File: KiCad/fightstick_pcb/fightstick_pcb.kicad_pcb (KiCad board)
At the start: 2 copper layers, 52 x 51 mm, 34 parts, among them J1 USB_B_Micro, J2 Conn_01x02, J3 Conn_02x18_Odd_Even, J4 Conn_02x18_Odd_Even, U1 NCP1117-3.3_SOT223, U2 W25Q128JVS, U3 RP2040, Y1 ABM8-272-T3

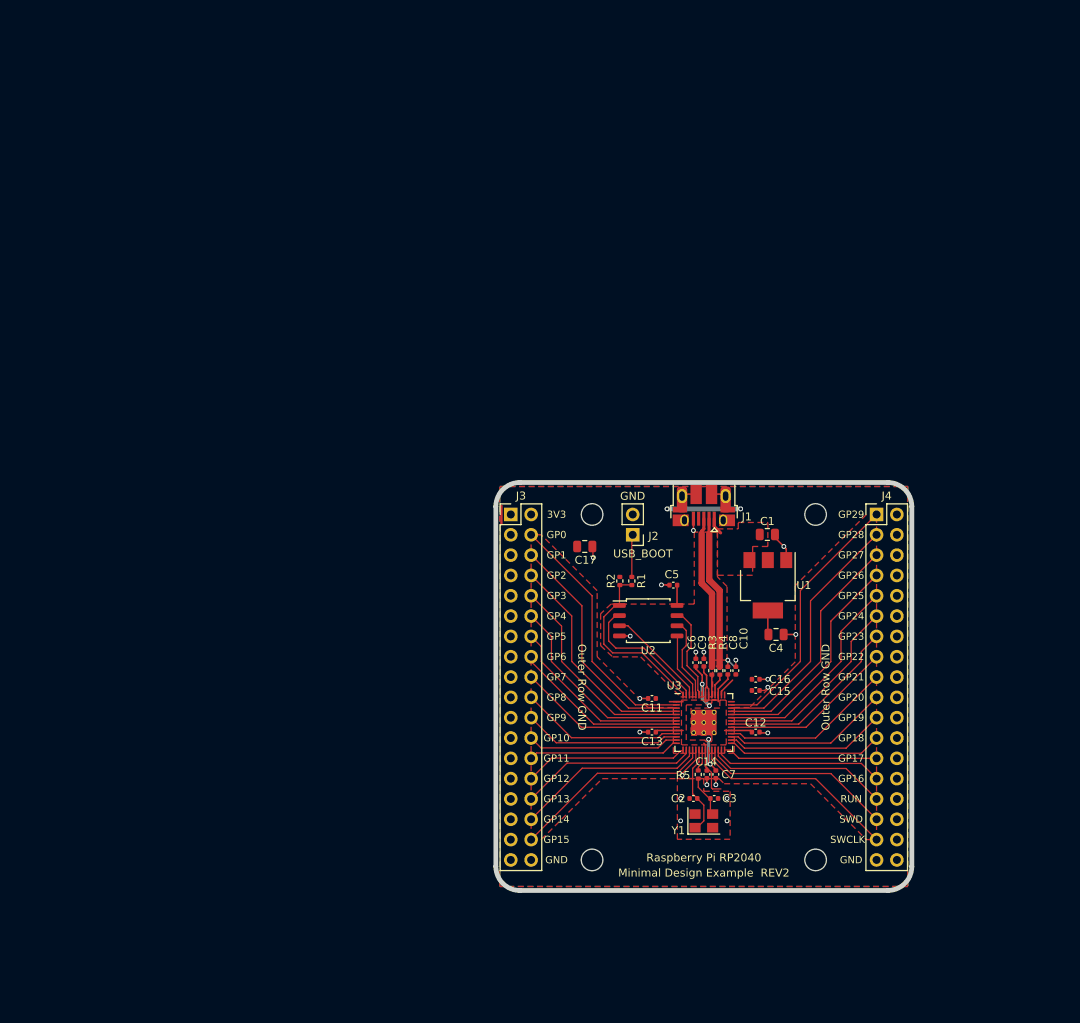
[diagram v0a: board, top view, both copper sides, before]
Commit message: Recreation of minimal design
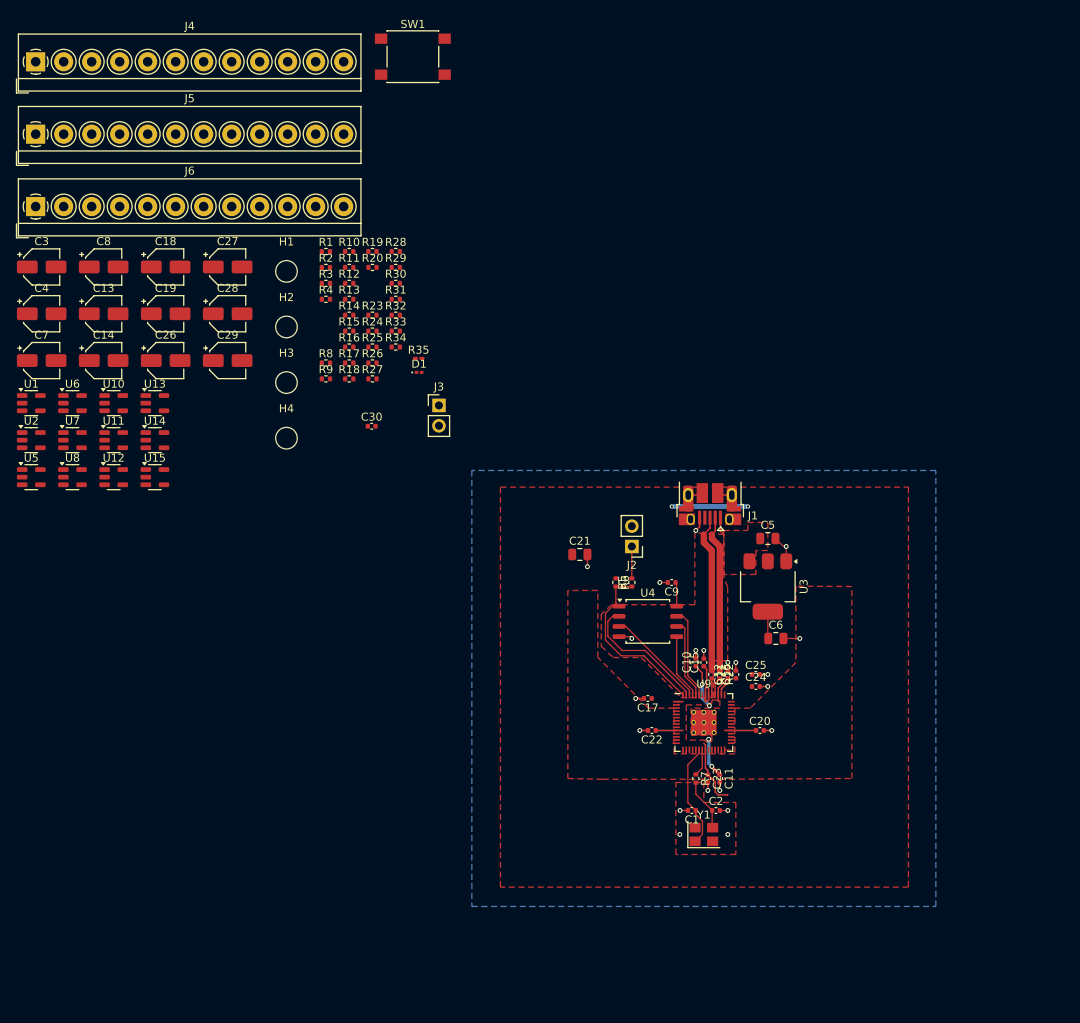
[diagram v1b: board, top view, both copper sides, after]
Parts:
- added C18: 1u, Capacitor_SMD:CP_Elec_4x3, F.Cu at (32.7, 43.1)
- added C19: 1u, Capacitor_SMD:CP_Elec_4x3, F.Cu at (32.7, 48.9)
- added C20: 100n, Capacitor_SMD:C_0402_1005Metric, F.Cu at (107.0, 101.0)
- added C21: 10u, Capacitor_SMD:C_0805_2012Metric, F.Cu at (84.5, 79.0)
- added C22: 100n, Capacitor_SMD:C_0402_1005Metric, F.Cu at (93.5, 101.0)
- added C23: 100n, Capacitor_SMD:C_0402_1005Metric, F.Cu at (100.5, 107.0)
- added C24: 100n, Capacitor_SMD:C_0402_1005Metric, F.Cu at (106.5, 95.5)
- added C25: 100n, Capacitor_SMD:C_0402_1005Metric, F.Cu at (106.5, 94.0)
- added C26: 1u, Capacitor_SMD:CP_Elec_4x3, F.Cu at (32.7, 54.8)
- added C27: 1u, Capacitor_SMD:CP_Elec_4x3, F.Cu at (40.5, 43.1)
- added C28: 1u, Capacitor_SMD:CP_Elec_4x3, F.Cu at (40.5, 48.9)
- added C29: 1u, Capacitor_SMD:CP_Elec_4x3, F.Cu at (40.5, 54.8)
- added C30: 100n, Capacitor_SMD:C_0402_1005Metric, F.Cu at (58.5, 63.0)
- added D1: GREEN, LED_SMD:LED_0201_0603Metric, F.Cu at (64.4, 56.2)
- added J5: Screw_Terminal_01x12, TerminalBlock_4Ucon:TerminalBlock_4Ucon_1x12_P3.50mm_Horizontal, F.Cu at (16.5, 26.5)
- added J6: Screw_Terminal_01x12, TerminalBlock_4Ucon:TerminalBlock_4Ucon_1x12_P3.50mm_Horizontal, F.Cu at (16.5, 35.5)
- added R10: 1k, Resistor_SMD:R_0402_1005Metric, F.Cu at (55.7, 41.1)
- added R11: 1k, Resistor_SMD:R_0402_1005Metric, F.Cu at (55.7, 43.1)
- added R12: 1k, Resistor_SMD:R_0402_1005Metric, F.Cu at (55.7, 45.1)
- added R13: 5.1k, Resistor_SMD:R_0402_1005Metric, F.Cu at (55.7, 47.1)
- added R14: 5.1k, Resistor_SMD:R_0402_1005Metric, F.Cu at (55.7, 49.1)
- added R15: 1k, Resistor_SMD:R_0402_1005Metric, F.Cu at (55.7, 51.1)
- added R16: 1k, Resistor_SMD:R_0402_1005Metric, F.Cu at (55.7, 53.1)
- added R17: 5.1k, Resistor_SMD:R_0402_1005Metric, F.Cu at (55.7, 55.1)
- added R18: 5.1k, Resistor_SMD:R_0402_1005Metric, F.Cu at (55.7, 57.0)
- added R19: 1k, Resistor_SMD:R_0402_1005Metric, F.Cu at (58.6, 41.1)
- added R20: 1k, Resistor_SMD:R_0402_1005Metric, F.Cu at (58.6, 43.1)
- added R21: 27, Resistor_SMD:R_0402_1005Metric, F.Cu at (101.0, 94.0)
- added R22: 27, Resistor_SMD:R_0402_1005Metric, F.Cu at (102.0, 94.0)
- added R23: 1k, Resistor_SMD:R_0402_1005Metric, F.Cu at (58.6, 49.1)
- added R24: 5.1k, Resistor_SMD:R_0402_1005Metric, F.Cu at (58.6, 51.1)
- added R25: 5.1k, Resistor_SMD:R_0402_1005Metric, F.Cu at (58.6, 53.1)
- added R26: 1k, Resistor_SMD:R_0402_1005Metric, F.Cu at (58.6, 55.1)
- added R27: 1k, Resistor_SMD:R_0402_1005Metric, F.Cu at (58.6, 57.0)
- added R28: 1k, Resistor_SMD:R_0402_1005Metric, F.Cu at (61.5, 41.1)
- added R29: 1k, Resistor_SMD:R_0402_1005Metric, F.Cu at (61.5, 43.1)
- added R30: 1k, Resistor_SMD:R_0402_1005Metric, F.Cu at (61.5, 45.1)
- added R31: 5.1k, Resistor_SMD:R_0402_1005Metric, F.Cu at (61.5, 47.1)
- added R32: 5.1k, Resistor_SMD:R_0402_1005Metric, F.Cu at (61.5, 49.1)
- added R33: 1k, Resistor_SMD:R_0402_1005Metric, F.Cu at (61.5, 51.1)
- added R34: 1k, Resistor_SMD:R_0402_1005Metric, F.Cu at (61.5, 53.1)
- added R35: 10k, Resistor_SMD:R_0201_0603Metric_Pad0.64x0.40mm_HandSolder, F.Cu at (64.3, 54.5)
- added R6: DNF, Resistor_SMD:R_0402_1005Metric, F.Cu at (89.0, 82.5)
- added R7: 1k, Resistor_SMD:R_0402_1005Metric, F.Cu at (99.0, 107.0)
- added R8: 5.1k, Resistor_SMD:R_0402_1005Metric, F.Cu at (52.8, 55.1)
- added R9: 5.1k, Resistor_SMD:R_0402_1005Metric, F.Cu at (52.8, 57.0)
- added SW1: SW_Push, Button_Switch_SMD:SW_Push_1P1T_NO_6x6mm_H9.5mm, F.Cu at (63.6, 16.8)
- added U10: SN74LVC1G14DBV, Package_TO_SOT_SMD:SOT-23-5, F.Cu at (26.2, 60.1)
- added U11: SN74LVC1G14DBV, Package_TO_SOT_SMD:SOT-23-5, F.Cu at (26.2, 64.7)
- added U12: SN74LVC1G14DBV, Package_TO_SOT_SMD:SOT-23-5, F.Cu at (26.2, 69.3)
- added U13: SN74LVC1G14DBV, Package_TO_SOT_SMD:SOT-23-5, F.Cu at (31.4, 60.1)
- added U14: SN74LVC1G14DBV, Package_TO_SOT_SMD:SOT-23-5, F.Cu at (31.4, 64.7)
- added U15: SN74LVC1G14DBV, Package_TO_SOT_SMD:SOT-23-5, F.Cu at (31.4, 69.3)
- added U4: W25Q128JVS, Package_SO:SOIC-8_5.23x5.23mm_P1.27mm, F.Cu at (93.0, 87.4)
- added U5: SN74LVC1G14DBV, Package_TO_SOT_SMD:SOT-23-5, F.Cu at (15.9, 69.3)
- added U6: SN74LVC1G14DBV, Package_TO_SOT_SMD:SOT-23-5, F.Cu at (21.1, 60.1)
- added U7: SN74LVC1G14DBV, Package_TO_SOT_SMD:SOT-23-5, F.Cu at (21.1, 64.7)
- added U8: SN74LVC1G14DBV, Package_TO_SOT_SMD:SOT-23-5, F.Cu at (21.1, 69.3)
- added U9: RP2040, RP2040_minimal:RP2040-QFN-56, F.Cu at (100.0, 100.0)
- C1: value 10u -> 15p; footprint Capacitor_SMD:C_0805_2012Metric -> Capacitor_SMD:C_0402_1005Metric
- C10: value 1u -> 100n
- C12, C16: value 100n -> 1u
- C13, C14, C7: value 100n -> 1u; footprint Capacitor_SMD:C_0402_1005Metric -> Capacitor_SMD:CP_Elec_4x3
- C17: value 10u -> 100n; footprint Capacitor_SMD:C_0805_2012Metric -> Capacitor_SMD:C_0402_1005Metric
- C3: value 15p -> 1u; footprint Capacitor_SMD:C_0402_1005Metric -> Capacitor_SMD:CP_Elec_4x3
- C4: value 10u -> 1u; footprint Capacitor_SMD:C_0805_2012Metric -> Capacitor_SMD:CP_Elec_4x3
- C5, C6: value 100n -> 10u; footprint Capacitor_SMD:C_0402_1005Metric -> Capacitor_SMD:C_0805_2012Metric
- C8: footprint Capacitor_SMD:C_0402_1005Metric -> Capacitor_SMD:CP_Elec_4x3
- J3: value Conn_02x18_Odd_Even -> Conn_01x02; footprint Connector_PinHeader_2.54mm:PinHeader_2x18_P2.54mm_Vertical -> Connector_PinHeader_2.54mm:PinHeader_1x02_P2.54mm_Vertical
- J4: value Conn_02x18_Odd_Even -> Screw_Terminal_01x12; footprint Connector_PinHeader_2.54mm:PinHeader_2x18_P2.54mm_Vertical -> TerminalBlock_4Ucon:TerminalBlock_4Ucon_1x12_P3.50mm_Horizontal
- R1: value 1k -> 5.1k
- R2: value DNF -> 5.1k
- R3, R4: value 27 -> 1k
- U1: value NCP1117-3.3_SOT223 -> SN74LVC1G14DBV; footprint Package_TO_SOT_SMD:SOT-223-3_TabPin2 -> Package_TO_SOT_SMD:SOT-23-5
- U2: value W25Q128JVS -> SN74LVC1G14DBV; footprint Package_SO:SOIC-8_5.23x5.23mm_P1.27mm -> Package_TO_SOT_SMD:SOT-23-5
- U3: value RP2040 -> NCP1117-3.3_SOT223; footprint RP2040_minimal:RP2040-QFN-56 -> Package_TO_SOT_SMD:SOT-223-3_TabPin2
- moved J4 119.4 mm to (16.5, 17.4)
- moved C3 107.2 mm to (17.2, 43.1)
- moved C4 100.2 mm to (17.2, 48.9)
- moved C7 98.9 mm to (17.2, 54.8), turned to 0 degrees
- moved U1 94.8 mm to (15.9, 60.1), turned to 0 degrees
- moved C8 92.9 mm to (25.0, 43.1), turned to 0 degrees
- moved C14 91.4 mm to (25.0, 54.8), turned to 0 degrees
- moved H3 89.1 mm to (47.8, 57.5)
- moved C13 86.2 mm to (25.0, 48.9), turned to 0 degrees
- moved U2 80.4 mm to (15.9, 64.7)
- moved H2 70.2 mm to (47.8, 50.6)
- moved R3 68.3 mm to (52.8, 45.1), turned to 0 degrees
- moved R4 67.7 mm to (52.8, 47.1), turned to 0 degrees
- moved H4 65.1 mm to (47.8, 64.5)
- moved R1 56.2 mm to (52.8, 41.1), turned to 0 degrees
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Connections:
- C1 pad 1: VBUS -> /XIN
- C10 pad 1: +3V3 -> +1V1
- C11 pad 1: +3V3 -> +1V1
- C12 pad 1: +3V3 -> +1V1
- C13 pad 1: +3V3 -> Net-(C13-Pad1)
- C14 pad 1: +3V3 -> Net-(C14-Pad1)
- C2 pad 1: /XIN -> Net-(C2-Pad1)
- C4 pad 1: +3V3 -> Net-(C4-Pad1)
- C5 pad 1: +3V3 -> VBUS
- C6 pad 1: +1V1 -> +3V3
- C7 pad 1: +1V1 -> Net-(C7-Pad1)
- C8 pad 1: +1V1 -> Net-(C8-Pad1)
- J3 pad 1: GND -> Net-(J3-Pin_1)
- J3 pad 2: +3V3 -> Net-(J3-Pin_2)
- J4 pad 1: /GPIO29_ADC3 -> /SW_1
- J4 pad 10: GND -> /SW_RT
- J4 pad 11: /GPIO24 -> /SW_B
- J4 pad 12: GND -> /SW_A
- J4 pad 2: GND -> /SW_0
- J4 pad 3: /GPIO28_ADC2 -> /SW_SELECT
- J4 pad 4: GND -> /SW_START
- J4 pad 5: /GPIO27_ADC1 -> /SW_LB
- J4 pad 6: GND -> /SW_RB
- J4 pad 7: /GPIO26_ADC0 -> /SW_Y
- J4 pad 8: GND -> /SW_X
- J4 pad 9: /GPIO25 -> /SW_LT
- R1 pad 1: /QSPI_SS -> +3V3
- R1 pad 2: /~{USB_BOOT} -> /SW_Y
- R2 pad 2: /QSPI_SS -> /SW_1
- R3 pad 1: /USB_D+ -> /SW_Y
- R3 pad 2: Net-(U3-USB_DP) -> Net-(C3-Pad1)
- R4 pad 1: /USB_D- -> /SW_1
- R4 pad 2: Net-(U3-USB_DM) -> Net-(C4-Pad1)
- R5 pad 1: /XOUT -> /QSPI_SS
- R5 pad 2: Net-(C3-Pad1) -> /~{USB_BOOT}
- U1 pad 1: GND -> unconnected-(U1-NC-Pad1)
- U1 pad 2: +3V3 -> Net-(C3-Pad1)
- U1 pad 3: VBUS -> GND
- U2 pad 1: /QSPI_SS -> unconnected-(U2-NC-Pad1)
- U2 pad 2: /QSPI_SD1 -> Net-(C4-Pad1)
- U2 pad 3: /QSPI_SD2 -> GND
- U2 pad 4: GND -> /SIG_1
- U2 pad 5: /QSPI_SD0 -> +3V3
- U3 pad 1: +3V3 -> GND
- U3 pad 2: /GPIO0 -> +3V3
- U3 pad 3: /GPIO1 -> VBUS
- Y1 pad 3: Net-(C3-Pad1) -> Net-(C2-Pad1)
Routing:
- net /GPIO29_ADC3: track 33.2 -> 0.00 mm
- net /GPIO0: track 31.8 -> 0.00 mm
- net /GPIO28_ADC2: track 31.6 -> 0.00 mm
- net /GPIO1: track 30.2 -> 0.00 mm
- net /GPIO27_ADC1: track 29.9 -> 0.00 mm
- net /GPIO2: track 28.5 -> 0.00 mm
- net /GPIO26_ADC0: track 28.3 -> 0.00 mm
- net /GPIO3: track 26.9 -> 0.00 mm
- net /GPIO25: track 26.7 -> 0.00 mm
- net /SWCLK: track 25.9 -> 0.00 mm
- net /GPIO15: track 25.4 -> 0.00 mm
- net /GPIO4: track 25.3 -> 0.00 mm
- net /GPIO24: track 25.0 -> 0.00 mm
- net /SWD: track 24.3 -> 0.00 mm
- net /GPIO14: track 23.8 -> 0.00 mm
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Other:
- board outline removed
- board text removed: "3V3"
- board text removed: "GND"
- board text removed: "GP0"
- board text removed: "GP1"
- board text removed: "GP10"
- board text removed: "GP11"
- board text removed: "GP12"
- board text removed: "GP13"
- board text removed: "GP14"
- board text removed: "GP15"
- board text removed: "GP16"
- board text removed: "GP17"
- board text removed: "GP18"
- board text removed: "GP19"
- board text removed: "GP2"
- board text removed: "GP20"
- board text removed: "GP21"
- board text removed: "GP22"
- board text removed: "GP23"
- board text removed: "GP24"
- board text removed: "GP25"
- board text removed: "GP26"
- board text removed: "GP27"
- board text removed: "GP28"
- board text removed: "GP29"
- board text removed: "GP3"
- board text removed: "GP4"
- board text removed: "GP5"
- board text removed: "GP6"
- board text removed: "GP7"
- board text removed: "GP8"
- board text removed: "GP9"
- board text removed: "Minimal Design Example REV2"
- board text removed: "Outer Row GND"
- board text removed: "RUN"
- board text removed: "Raspberry Pi RP2040"
- board text removed: "SWCLK"
- board text removed: "SWD"
- board text removed: "USB_BOOT"

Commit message: Les circuits de debounce sont settés
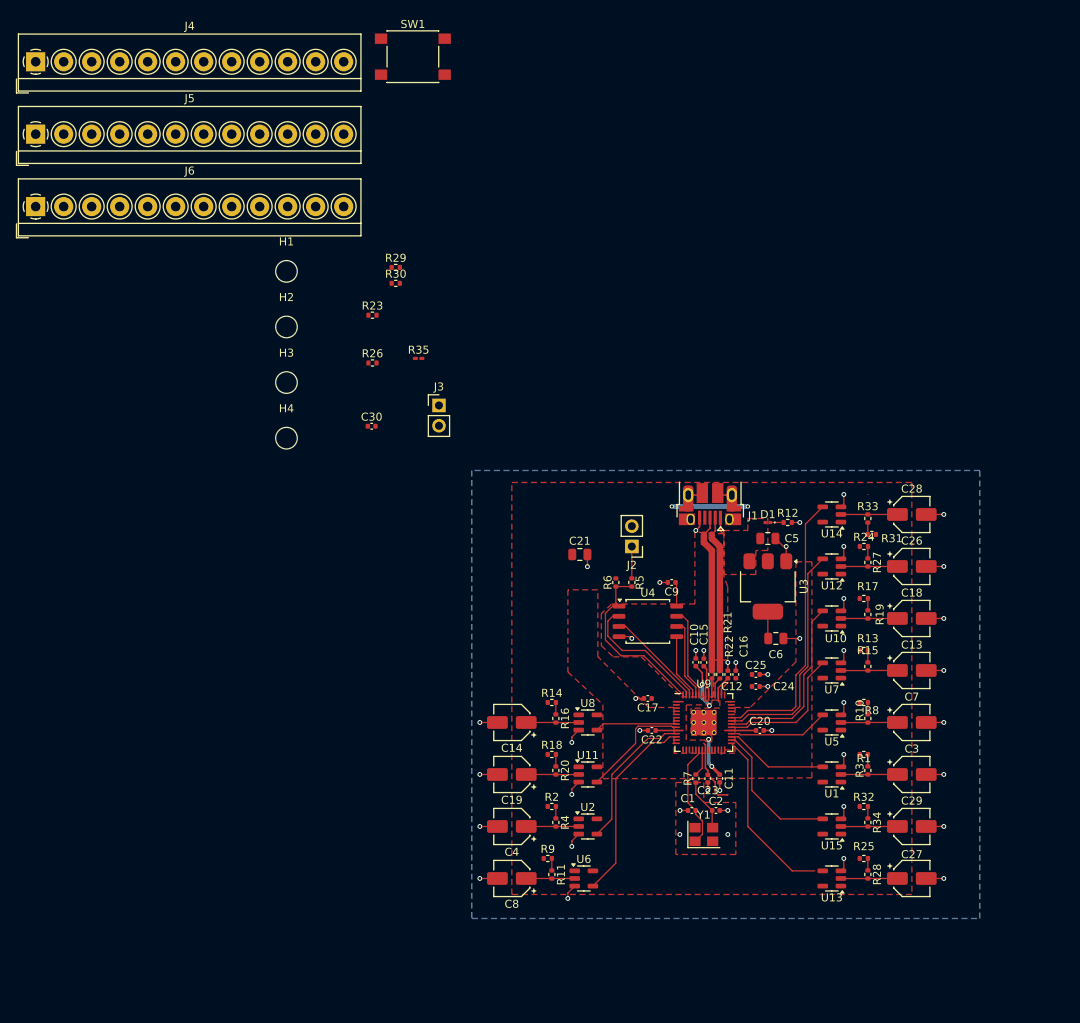
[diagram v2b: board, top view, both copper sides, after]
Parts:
- moved C3 125.9 mm to (126.0, 106.5)
- moved C7 117.8 mm to (126.0, 100.0)
- moved C27 114.7 mm to (126.0, 119.5)
- moved C13 110.4 mm to (126.0, 93.5)
- moved U1 110.3 mm to (116.0, 106.5), turned to 180 degrees
- moved U5 104.7 mm to (116.0, 100.0), turned to 180 degrees
- moved C29 103.5 mm to (126.0, 113.0)
- moved U13 103.4 mm to (116.0, 119.5), turned to 180 degrees
- moved C18 103.1 mm to (126.0, 87.0)
- moved U7 99.2 mm to (116.0, 93.5), turned to 180 degrees
- moved R28 97.7 mm to (120.5, 119.0), turned to -90 degrees
- moved C26 96.8 mm to (126.0, 80.5)
- moved U15 95.2 mm to (116.0, 113.0), turned to 180 degrees
- moved U10 93.7 mm to (116.0, 87.0), turned to 180 degrees
- moved R1 92.1 mm to (120.0, 104.0)
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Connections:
- U9 pad 13: /SIG_SELECT -> unconnected-(U9-GPIO10-Pad13)
- U9 pad 14: /SIG_START -> unconnected-(U9-GPIO11-Pad14)
- U9 pad 8: unconnected-(U9-GPIO6-Pad8) -> /SIG_SELECT
- U9 pad 9: unconnected-(U9-GPIO7-Pad9) -> /SIG_START
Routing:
- net GND: track 28.5 -> 77.2 mm, vias 21 -> 46
- net /SIG_A: track 0.00 -> 35.0 mm
- net /SIG_B: track 0.00 -> 28.9 mm
- net /SIG_0: track 0.00 -> 24.4 mm
- net /SIG_RT: track 0.00 -> 22.9 mm
- net /SIG_LB: track 0.40 -> 21.9 mm
- net /SIG_1: track 0.00 -> 18.4 mm
- net /SIG_RB: track 0.00 -> 18.0 mm
- net /SIG_LT: track 0.00 -> 17.2 mm
- net /SIG_START: track 0.43 -> 13.9 mm
- net /SIG_Y: track 0.00 -> 13.0 mm
- net /SIG_X: track 0.00 -> 12.5 mm
- net /SIG_SELECT: track 0.00 -> 10.3 mm
- net Net-(C7-Pad1): track 0.00 -> 7.07 mm
- net Net-(C27-Pad1): track 0.00 -> 7.07 mm
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
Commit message: PCB Fightstick V1
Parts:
- added G***: LOGO, LOGO, F.Cu at (66.5, 122.5)
- added REF**: KiCad-Logo2_5mm_SilkScreen, Symbol:KiCad-Logo2_5mm_SilkScreen, B.Cu at (72.0, 122.5)
- added REF**: WEEE-Logo_4.2x6mm_SilkScreen, Symbol:WEEE-Logo_4.2x6mm_SilkScreen, B.Cu at (74.0, 130.0)
- C30: footprint Capacitor_SMD:C_0402_1005Metric -> Capacitor_SMD:C_0805_2012Metric
- D1: footprint LED_SMD:LED_0201_0603Metric -> LED_SMD:LED_0805_2012Metric
- R1, R10, R11, R12, R13, R14, R15, R16, R17, R18, R19, R2, R20, R23, R24, R25, R26, R27, R28, R29, R3, R30, R31, R32, R33, R34, R4, R8, R9: footprint Resistor_SMD:R_0402_1005Metric -> Resistor_SMD:R_0805_2012Metric
- R35: footprint Resistor_SMD:R_0201_0603Metric_Pad0.64x0.40mm_HandSolder -> Resistor_SMD:R_0805_2012Metric
- moved J4 154.8 mm to (137.0, 114.5), turned to 90 degrees
- moved H1 124.5 mm to (137.0, 130.5)
- moved J5 123.0 mm to (82.0, 130.5)
- moved SW1 111.8 mm to (104.0, 121.0)
- moved H2 91.0 mm to (137.0, 68.5)
- moved R23 89.3 mm to (130.9, 101.5), turned to 180 degrees
- moved R26 78.4 mm to (130.6, 86.0), turned to 180 degrees
- moved R35 74.3 mm to (97.0, 121.2), turned to -90 degrees
- moved C30 71.0 mm to (94.0, 124.5), turned to 180 degrees
- moved H4 68.4 mm to (65.5, 130.5)
- moved C29 63.7 mm to (76.0, 73.5), turned to 180 degrees
- moved J6 63.3 mm to (65.5, 75.5), turned to -90 degrees
- moved J3 63.0 mm to (89.5, 119.2)
- moved C27 62.5 mm to (76.0, 82.0), turned to 180 degrees
- moved R30 56.7 mm to (71.0, 101.0), turned to -90 degrees
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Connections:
- J4 pad 1: /SW_1 -> /SIG_STICK_0
- J4 pad 10: /SW_RT -> /LED_P1+
- J4 pad 2: /SW_0 -> /SIG_STICK_1
- J4 pad 3: /SW_SELECT -> /SW_Y
- J4 pad 4: /SW_START -> /SW_X
- J4 pad 5: /SW_LB -> /LED_P0-
- J4 pad 6: /SW_RB -> /LED_P0+
- J4 pad 7: /SW_Y -> /SW_LT
- J4 pad 8: /SW_X -> /SW_RT
- J4 pad 9: /SW_LT -> /LED_P1-
- J6 pad 10: /LED_P0- -> /SW_1
- J6 pad 11: /LED_P0+ -> /SW_0
- J6 pad 2: /SIG_STICK_1 -> /SW_RB
- J6 pad 3: /SIG_STICK_0 -> /SW_LB
- J6 pad 4: /LED_P3- -> /LED_P2-
- J6 pad 5: /LED_P3+ -> /LED_P2+
- J6 pad 6: /LED_P2- -> /SW_SELECT
- J6 pad 7: /LED_P2+ -> /SW_START
- J6 pad 8: /LED_P1- -> /LED_P3-
- J6 pad 9: /LED_P1+ -> /LED_P3+
- U9 pad 11: /SIG_1 -> /SIG_START
- U9 pad 12: /SIG_0 -> /SIG_1
- U9 pad 13: unconnected-(U9-GPIO10-Pad13) -> /SIG_0
- U9 pad 2: /LED_P0+ -> unconnected-(U9-GPIO0-Pad2)
- U9 pad 29: /SIG_LB -> unconnected-(U9-GPIO18-Pad29)
- U9 pad 3: /LED_P1+ -> /SIG_RB
- U9 pad 30: /SIG_RB -> unconnected-(U9-GPIO19-Pad30)
- U9 pad 4: /LED_P2+ -> /SIG_LB
- U9 pad 5: /LED_P3+ -> /LED_P0+
- U9 pad 6: unconnected-(U9-GPIO4-Pad6) -> /LED_P1+
- U9 pad 7: unconnected-(U9-GPIO5-Pad7) -> /LED_P2+
- U9 pad 8: /SIG_SELECT -> /LED_P3+
- U9 pad 9: /SIG_START -> /SIG_SELECT
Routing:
- net /LED_P1+: track 0.00 -> 55.6 mm, vias 0 -> 1
- net /LED_P0+: track 0.00 -> 53.3 mm, vias 0 -> 1
- net /SIG_STICK_0: track 0.00 -> 40.4 mm, vias 0 -> 1
- net /SIG_STICK_1: track 0.00 -> 39.6 mm, vias 0 -> 1
- net /RUN: track 0.00 -> 35.6 mm
- net /LED_P2+: track 0.00 -> 35.3 mm, vias 0 -> 1
- net /LED_P3+: track 0.00 -> 34.3 mm, vias 0 -> 1
- net Net-(J3-Pin_2): track 0.00 -> 32.4 mm, vias 0 -> 2
- net Net-(J3-Pin_1): track 0.00 -> 29.0 mm, vias 0 -> 2
- net /SW_Y: track 1.49 -> 25.1 mm, vias 0 -> 2
- net +3V3: track 42.2 -> 64.9 mm
- net /SW_RB: track 1.49 -> 22.6 mm
- net GND: track 77.2 -> 98.2 mm, vias 46 -> 55
- net /SW_B: track 1.50 -> 21.6 mm, vias 0 -> 1
- net /SW_SELECT: track 1.49 -> 21.5 mm
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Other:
- board outline added: 80.5 x 70 mm
- board text added: "FIGHTSTICK PCB"
